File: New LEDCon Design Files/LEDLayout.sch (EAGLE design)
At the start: 23 parts

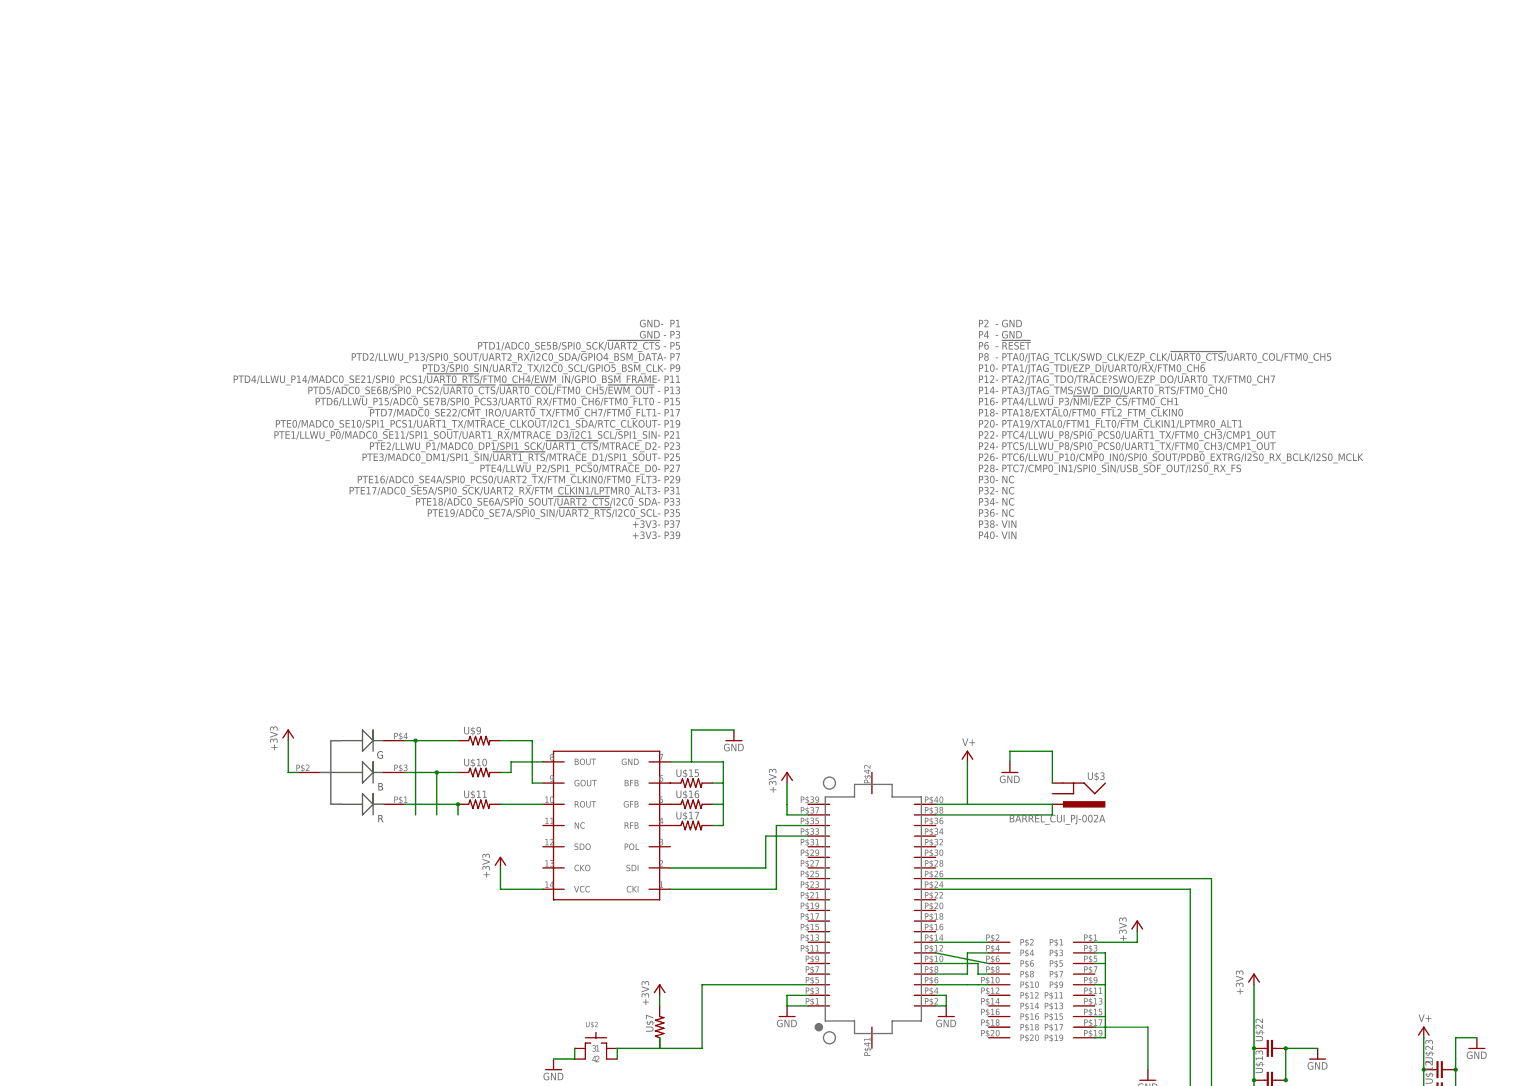
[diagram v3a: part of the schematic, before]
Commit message: Prototype 4
Fixed LED, removed jumpers, fixed JTAG traces and added RA reset button
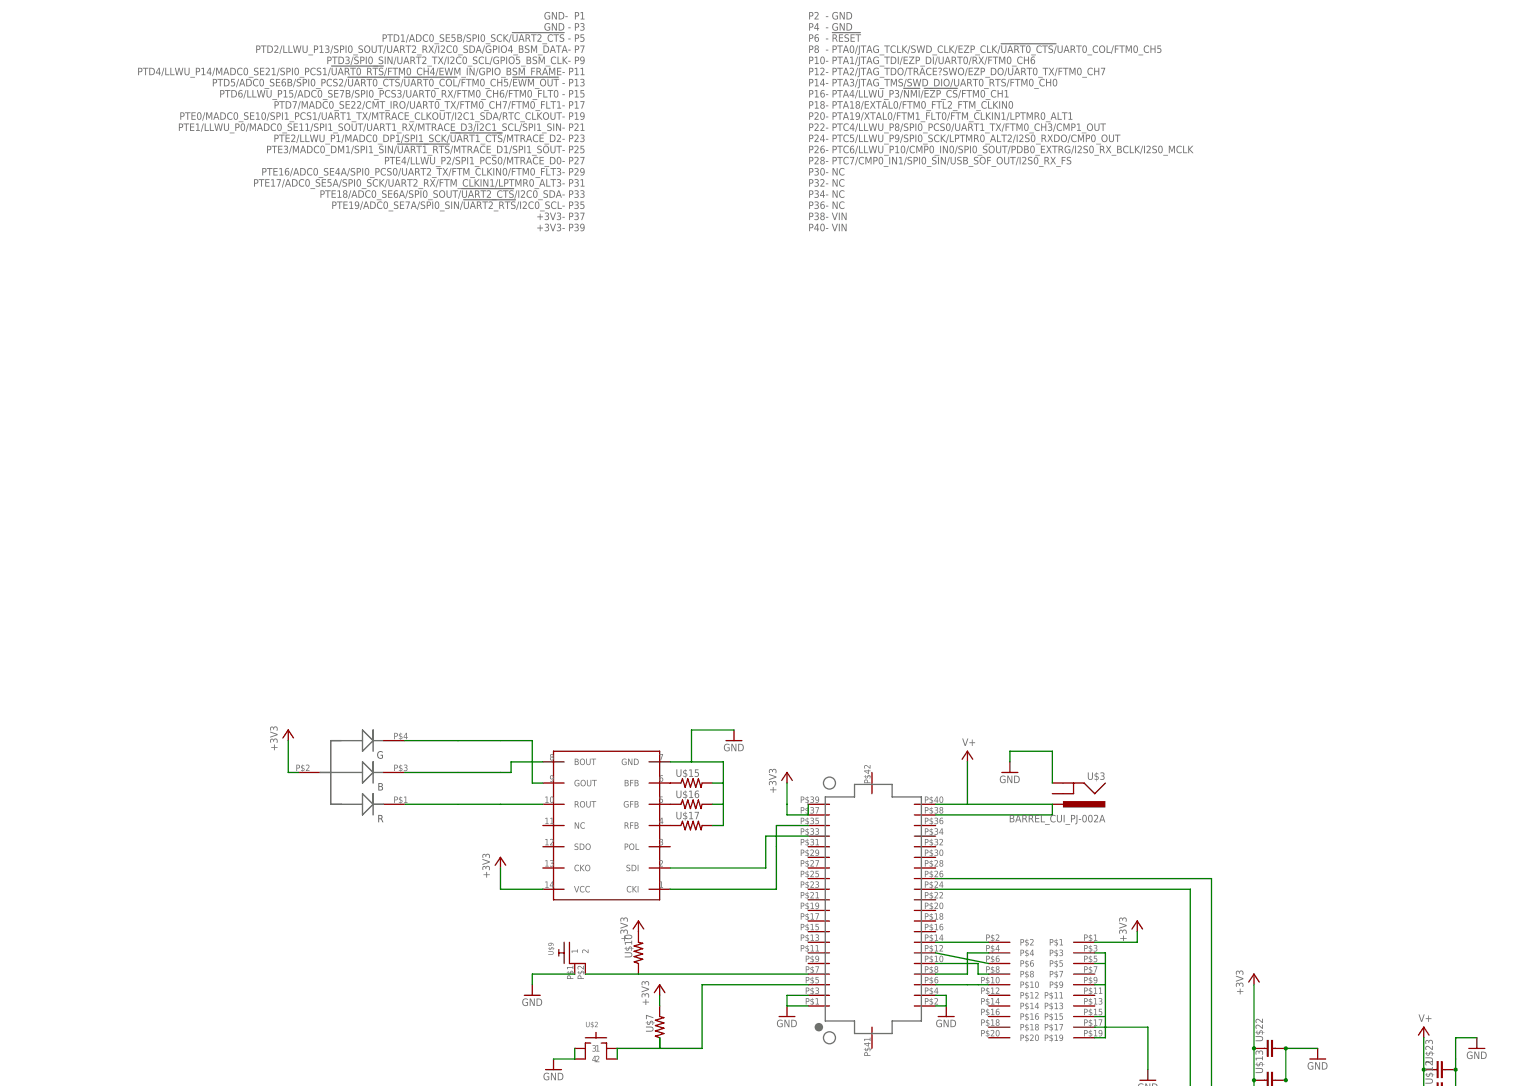
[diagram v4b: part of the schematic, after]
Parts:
- removed U$11: (no value), GW-devices:RF-R0805
- U$9: value (none) -> RA_BUTTON; device GW-devices:RF-R0805 -> KW2:RA_BUTTON
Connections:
- removed net N$19: U$4.PTA3/JTAG_TMS/SWD_DIO/UART0_RTS/FTM0_CH0
- removed net N$22: U$4.PTA2/JTAG_TDO/TRACE?SWO/EZP_DO/UART0_TX/FTM0_CH7
- net +3V3: now also U$10.2, U$4.+3V3@2
- net GND: now also U$9.1
- net N$4: now also U$8.GOUT; no longer U$9.1
- net N$5: now also U$8.BOUT; no longer U$10.1
- net N$6: now also U$19.P$2, U$4.PTA3/JTAG_TMS/SWD_DIO/UART0_RTS/FTM0_CH0; no longer U$11.2, U$8.ROUT
- net N$7: now also U$8.ROUT; no longer U$11.1
- net N$8: now also U$19.P$6, U$4.PTA2/JTAG_TDO/TRACE?SWO/EZP_DO/UART0_TX/FTM0_CH7; no longer U$10.2, U$8.BOUT
- net N$9: now also U$10.1, U$4.PTD2/LLWU_P13/SPI0_SOUT/UART2_RX/I2C0_SDA/GPIO4_BSM_DATA; no longer U$8.GOUT
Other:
- moved on the sheet: U$10
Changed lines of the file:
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@@
 <part name="+3V5" library="supply1" deviceset="+3V3" device=""/>
 <part name="U$8" library="GW-devices" deviceset="WS2801" device=""/>
-<part name="U$9" library="GW-devices" deviceset="RF-R" device="0805"/>
-<part name="U$10" library="GW-devices" deviceset="RF-R" device="0805"/>
-<part name="U$11" library="GW-devices" deviceset="RF-R" device="0805"/>
 <part name="GND7" library="supply1" deviceset="GND" device=""/>
 <part name="+3V6" library="supply1" deviceset="+3V3" device=""/>
@@
 <part name="U$22" library="GW-devices" deviceset="RF-C" device="0805"/>
 <part name="U$23" library="GW-devices" deviceset="RF-C" device="0805"/>
+<part name="U$9" library="KW2" deviceset="RA_BUTTON" device=""/>
+<part name="GND11" library="supply1" deviceset="GND" device=""/>
+<part name="U$10" library="GW-devices" deviceset="RF-R" device="0805"/>
+<part name="+3V8" library="supply1" deviceset="+3V3" device=""/>
 </parts>
 <sheets>
@@
 <instance part="+3V5" gate="G$1" x="-129.54" y="25.4"/>
 <instance part="U$8" gate="G$1" x="-55.88" y="2.54" rot="R180"/>
-<instance part="U$9" gate="G$1" x="-83.82" y="22.86"/>
-<instance part="U$10" gate="G$1" x="-83.82" y="15.24"/>
-<instance part="U$11" gate="G$1" x="-83.82" y="7.62"/>
 <instance part="GND7" gate="1" x="-22.86" y="22.86"/>
 <instance part="+3V6" gate="G$1" x="-78.74" y="-5.08"/>
@@
 <instance part="U$22" gate="G$1" x="104.14" y="-50.8" rot="R90"/>
 <instance part="U$23" gate="G$1" x="144.78" y="-55.88" rot="R90"/>
+<instance part="U$9" gate="G$1" x="-60.96" y="-33.02" rot="MR0"/>
+<instance part="GND11" gate="1" x="-71.12" y="-38.1"/>
+<instance part="U$10" gate="G$1" x="-45.72" y="-27.94" smashed="yes" rot="R90">
+<attribute name="NAME" x="-47.2186" y="-29.21" size="1.778" layer="95" rot="R90"/>
+<attribute name="VALUE" x="-42.418" y="-31.75" size="1.778" layer="96" rot="R90"/>
+</instance>
+<instance part="+3V8" gate="G$1" x="-45.72" y="-20.32"/>
 </instances>
 <busses>
@@
 <junction x="109.22" y="-50.8"/>
 </segment>
+<segment>
+<pinref part="U$9" gate="G$1" pin="1"/>
+<pinref part="GND11" gate="1" pin="GND"/>
+<wire x1="-60.96" y1="-33.02" x2="-71.12" y2="-33.02" width="0.1524" layer="91"/>
+<wire x1="-71.12" y1="-33.02" x2="-71.12" y2="-35.56" width="0.1524" layer="91"/>
+</segment>
 </net>
 <net name="+3V3" class="0">
@@
 <wire x1="-5.08" y1="5.08" x2="-10.16" y2="5.08" width="0.1524" layer="91"/>
 <wire x1="-10.16" y1="5.08" x2="-10.16" y2="7.62" width="0.1524" layer="91"/>
+<pinref part="U$4" gate="G$1" pin="+3V3@2"/>
+<wire x1="-5.08" y1="7.62" x2="-5.08" y2="5.08" width="0.1524" layer="91"/>
 </segment>
 <segment>
@@
 </segment>
 <segment>
-<pinref part="U$5" gate="G$1" pin="ANODE"/>
-<wire x1="-127" y1="15.24" x2="-129.54" y2="15.24" width="0.1524" layer="91"/>
 <pinref part="+3V5" gate="G$1" pin="+3V3"/>
 <wire x1="-129.54" y1="15.24" x2="-129.54" y2="22.86" width="0.1524" layer="91"/>
+<pinref part="U$5" gate="G$1" pin="ANODE"/>
+<wire x1="-129.54" y1="15.24" x2="-127" y2="15.24" width="0.1524" layer="91"/>
 </segment>
 <segment>
@@
 <pinref part="U$19" gate="G$1" pin="P$1"/>
 <wire x1="73.66" y1="-25.4" x2="63.5" y2="-25.4" width="0.1524" layer="91"/>
+</segment>
+<segment>
+<pinref part="U$10" gate="G$1" pin="2"/>
+<pinref part="+3V8" gate="G$1" pin="+3V3"/>
 </segment>
 </net>
@@
 <net name="N$4" class="0">
 <segment>
+<wire x1="-78.74" y1="22.86" x2="-71.12" y2="22.86" width="0.1524" layer="91"/>
+<wire x1="-71.12" y1="22.86" x2="-71.12" y2="12.7" width="0.1524" layer="91"/>
+<pinref part="U$8" gate="G$1" pin="GOUT"/>
+<wire x1="-71.12" y1="12.7" x2="-68.58" y2="12.7" width="0.1524" layer="91"/>
+<wire x1="-88.9" y1="22.86" x2="-78.74" y2="22.86" width="0.1524" layer="91"/>
 <pinref part="U$5" gate="G$1" pin="GREEN"/>
-<wire x1="-101.6" y1="22.86" x2="-99.06" y2="22.86" width="0.1524" layer="91"/>
-<pinref part="U$9" gate="G$1" pin="1"/>
-<wire x1="-99.06" y1="22.86" x2="-88.9" y2="22.86" width="0.1524" layer="91"/>
-<wire x1="-99.06" y1="5.08" x2="-99.06" y2="22.86" width="0.1524" layer="91"/>
-<junction x="-99.06" y="22.86"/>
+<wire x1="-88.9" y1="22.86" x2="-101.6" y2="22.86" width="0.1524" layer="91"/>
 </segment>
 </net>
 <net name="N$5" class="0">
 <segment>
-<pinref part="U$5" gate="G$1" pin="BLUE"/>
-<wire x1="-101.6" y1="15.24" x2="-93.98" y2="15.24" width="0.1524" layer="91"/>
-<pinref part="U$10" gate="G$1" pin="1"/>
-<wire x1="-93.98" y1="15.24" x2="-88.9" y2="15.24" width="0.1524" layer="91"/>
-<wire x1="-93.98" y1="5.08" x2="-93.98" y2="15.24" width="0.1524" layer="91"/>
-<junction x="-93.98" y="15.24"/>
-</segment>
-</net>
-<net name="N$7" class="0">
-<segment>
-<pinref part="U$11" gate="G$1" pin="1"/>
-<wire x1="-88.9" y1="5.08" x2="-88.9" y2="7.62" width="0.1524" layer="91"/>
-<pinref part="U$5" gate="G$1" pin="RED"/>
-<wire x1="-101.6" y1="7.62" x2="-88.9" y2="7.62" width="0.1524" layer="91"/>
-<junction x="-88.9" y="7.62"/>
-</segment>
-</net>
-<net name="N$6" class="0">
-<segment>
-<pinref part="U$11" gate="G$1" pin="2"/>
-<pinref part="U$8" gate="G$1" pin="ROUT"/>
-<wire x1="-78.74" y1="7.62" x2="-68.58" y2="7.62" width="0.1524" layer="91"/>
-</segment>
-</net>
-<net name="N$8" class="0">
-<segment>
-<pinref part="U$10" gate="G$1" pin="2"/>
 <wire x1="-78.74" y1="15.24" x2="-76.2" y2="15.24" width="0.1524" layer="91"/>
 <wire x1="-76.2" y1="15.24" x2="-76.2" y2="17.78" width="0.1524" layer="91"/>
 <pinref part="U$8" gate="G$1" pin="BOUT"/>
 <wire x1="-76.2" y1="17.78" x2="-68.58" y2="17.78" width="0.1524" layer="91"/>
-</segment>
-</net>
-<net name="N$9" class="0">
-<segment>
-<pinref part="U$9" gate="G$1" pin="2"/>
-<wire x1="-78.74" y1="22.86" x2="-71.12" y2="22.86" width="0.1524" layer="91"/>
-<wire x1="-71.12" y1="22.86" x2="-71.12" y2="12.7" width="0.1524" layer="91"/>
-<pinref part="U$8" gate="G$1" pin="GOUT"/>
-<wire x1="-71.12" y1="12.7" x2="-68.58" y2="12.7" width="0.1524" layer="91"/>
+<wire x1="-88.9" y1="15.24" x2="-78.74" y2="15.24" width="0.1524" layer="91"/>
+<pinref part="U$5" gate="G$1" pin="BLUE"/>
+<wire x1="-88.9" y1="15.24" x2="-101.6" y2="15.24" width="0.1524" layer="91"/>
+</segment>
+</net>
+<net name="N$7" class="0">
+<segment>
+<pinref part="U$8" gate="G$1" pin="ROUT"/>
+<wire x1="-78.74" y1="7.62" x2="-68.58" y2="7.62" width="0.1524" layer="91"/>
+<wire x1="-88.9" y1="7.62" x2="-78.74" y2="7.62" width="0.1524" layer="91"/>
+<pinref part="U$5" gate="G$1" pin="RED"/>
+<wire x1="-88.9" y1="7.62" x2="-101.6" y2="7.62" width="0.1524" layer="91"/>
 </segment>
 </net>
@@
 </segment>
 </net>
-<net name="N$19" class="0">
-<segment>
-<pinref part="U$4" gate="G$1" pin="PTA3/JTAG_TMS/SWD_DIO/UART0_RTS/FTM0_CH0"/>
-<wire x1="25.4" y1="-25.4" x2="38.1" y2="-25.4" width="0.1524" layer="91"/>
-</segment>
-</net>
 <net name="N$18" class="0">
 <segment>
@@
 </segment>
 </net>
-<net name="N$22" class="0">
+<net name="N$6" class="0">
+<segment>
+<pinref part="U$4" gate="G$1" pin="PTA3/JTAG_TMS/SWD_DIO/UART0_RTS/FTM0_CH0"/>
+<pinref part="U$19" gate="G$1" pin="P$2"/>
+<wire x1="25.4" y1="-25.4" x2="38.1" y2="-25.4" width="0.1524" layer="91"/>
+</segment>
+</net>
+<net name="N$8" class="0">
 <segment>
 <pinref part="U$4" gate="G$1" pin="PTA2/JTAG_TDO/TRACE?SWO/EZP_DO/UART0_TX/FTM0_CH7"/>
+<pinref part="U$19" gate="G$1" pin="P$6"/>
 <wire x1="25.4" y1="-27.94" x2="38.1" y2="-30.48" width="0.1524" layer="91"/>
 </segment>
 </net>
+<net name="N$9" class="0">
+<segment>
+<pinref part="U$9" gate="G$1" pin="2"/>
+<pinref part="U$4" gate="G$1" pin="PTD2/LLWU_P13/SPI0_SOUT/UART2_RX/I2C0_SDA/GPIO4_BSM_DATA"/>
+<wire x1="-58.42" y1="-33.02" x2="-45.72" y2="-33.02" width="0.1524" layer="91"/>
+<pinref part="U$10" gate="G$1" pin="1"/>
+<wire x1="-45.72" y1="-33.02" x2="-5.08" y2="-33.02" width="0.1524" layer="91"/>
+</segment>
+</net>

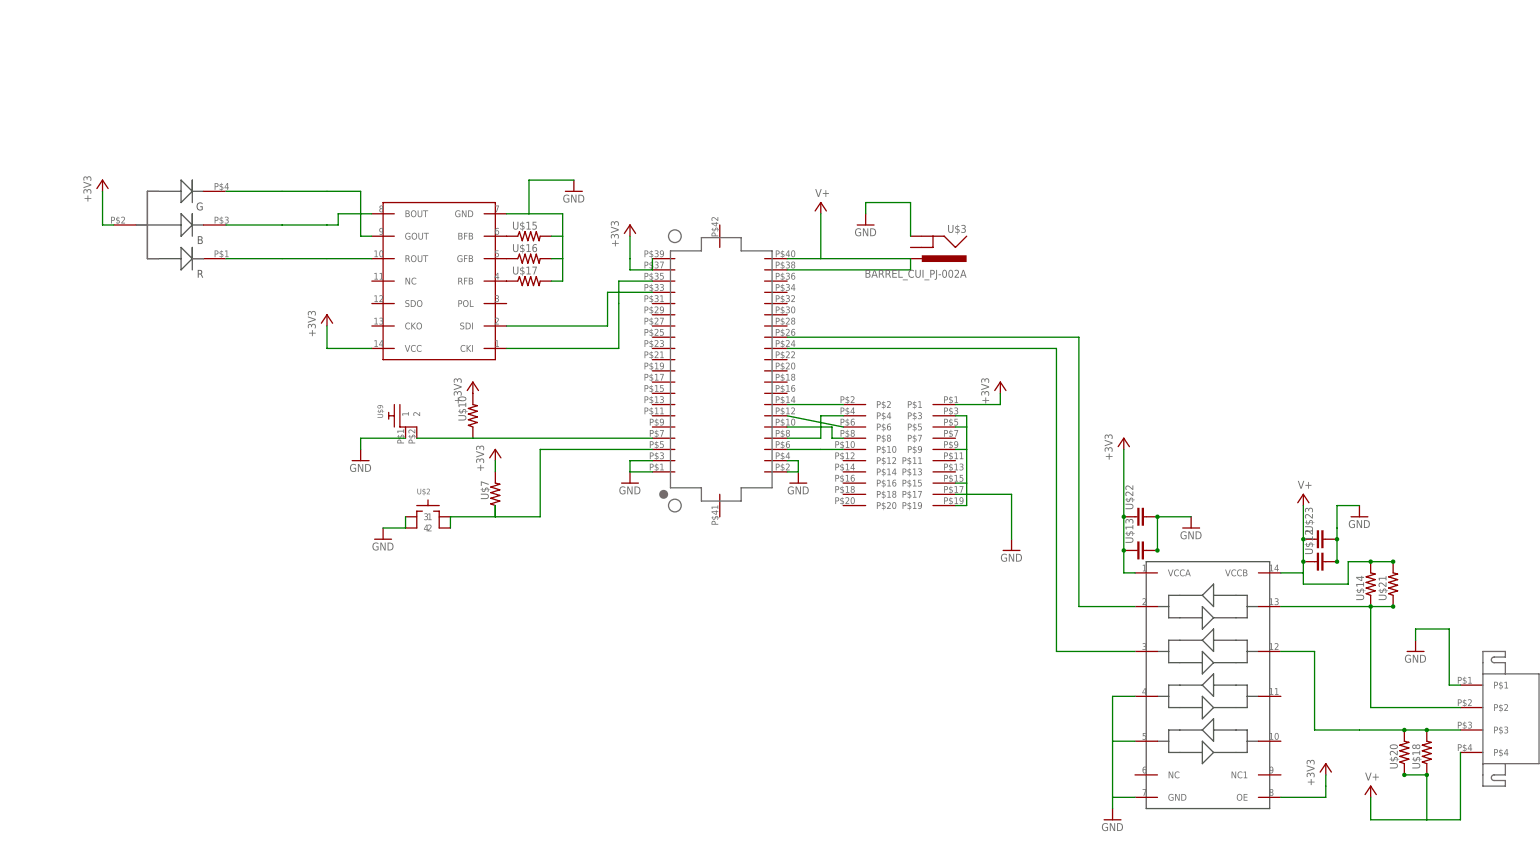
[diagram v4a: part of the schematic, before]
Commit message: Prototype 5
Added Vreg, caps, fixed LED, assigned values & PNs, removed 0402
footprints. Pending exporting of production files
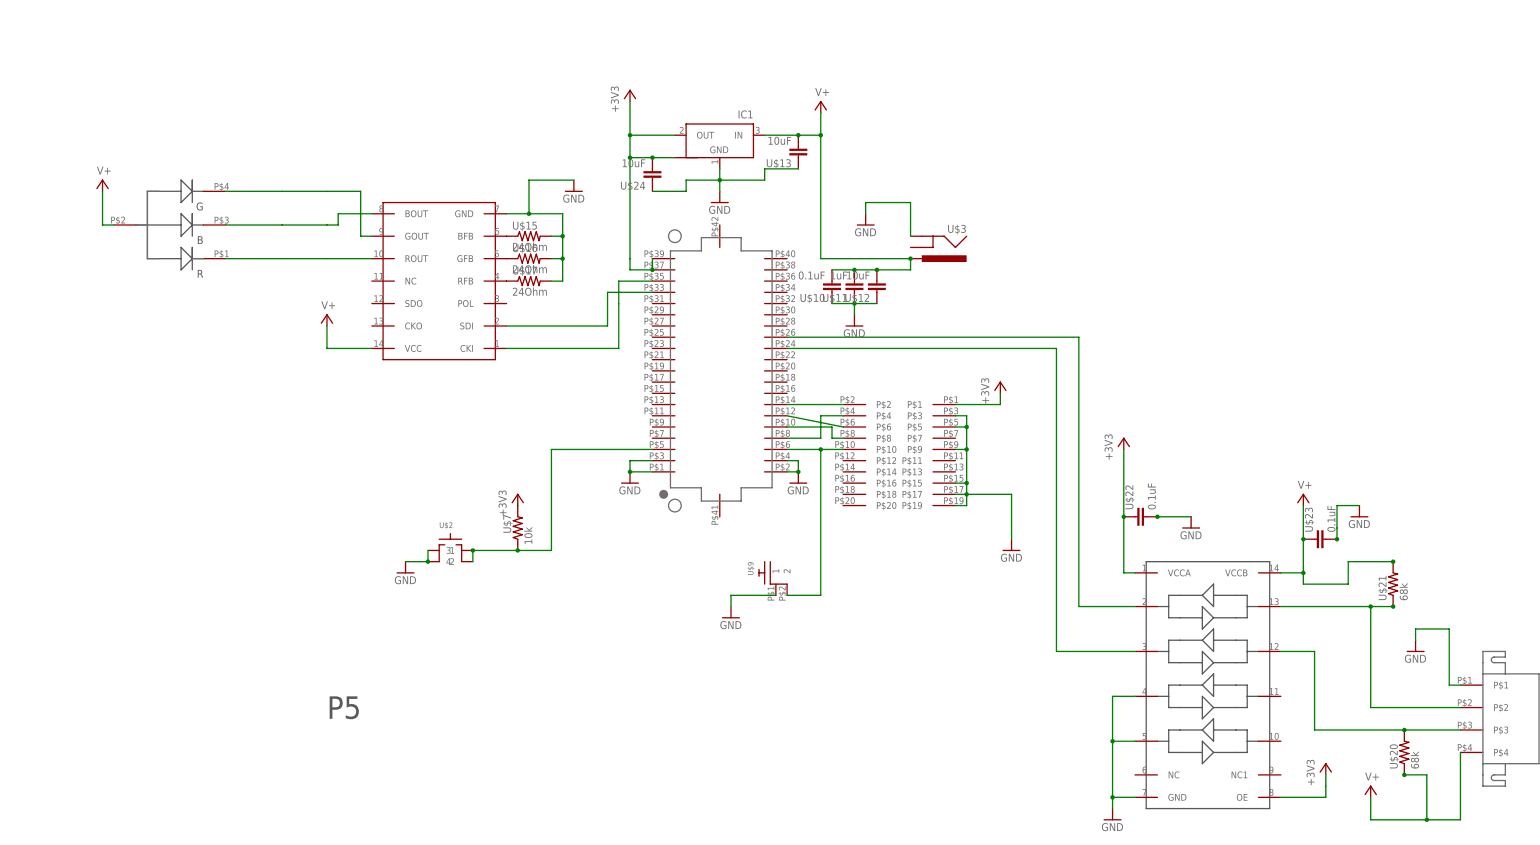
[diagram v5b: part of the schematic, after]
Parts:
- removed U$14, U$18: (no value), GW-devices:RF-R0402
- added IC1: (no value), KW2:NCP1117ST33T3G_1
- added U$11: 1uF, GW-devices:RF-C0805
- added U$24: 10uF, GW-devices:RF-C0805
- U$1: MFGN (none) -> TE Connectivity; MFGP (none) -> 643230-1
- U$10: value (none) -> 0.1uF; device GW-devices:RF-R0805 -> GW-devices:RF-C0805; MFGN (none) -> TDK; MFGP (none) -> C2012X5R1H104K085AA
- U$12, U$13: value (none) -> 10uF; device GW-devices:RF-C0402 -> GW-devices:RF-C0805; MFGN (none) -> Murata; MFGP (none) -> GRM219R61E106KA12D
- U$15, U$16, U$17: value (none) -> 24Ohm; MFGN (none) -> Vishay Dale; MFGP (none) -> CRCW080524R0FKEA
- U$2: MFGN (none) -> E-Switch; MFGP (none) -> TL3301PF160QG
- U$20, U$21: value (none) -> 68k; MFGN (none) -> Vishay Dale; MFGP (none) -> CRCW080568K0FKEA
- U$22, U$23: value (none) -> 0.1uF; MFGN (none) -> TDK; MFGP (none) -> C2012X5R1H104K085AA
- U$4: MFGN (none) -> Hirose; MFGP (none) -> DF12(3.0)-40DP-0.5V(86)
- U$5: MFGN Cree, Inc -> (none); MFGP CLV1A-FKB-CK1N1G1BB7R4S3 -> (none)
- U$6: MFGN (none) -> Texas Instruments
- U$7: value (none) -> 10k; MFGN (none) -> Vishay Dale; MFGP (none) -> CRCW080510K0FKEA
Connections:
- removed net N$21 (its old number): U$19.P$10, U$4.!RESET
- removed net N$9: U$10.1, U$4.PTD2/LLWU_P13/SPI0_SOUT/UART2_RX/I2C0_SDA/GPIO4_BSM_DATA, U$9.2
- new net N$3: U$19.P$10, U$4.!RESET, U$9.2
- net +3V3: now also IC1.OUT, IC1.OUT1, U$24.2; no longer U$10.2, U$13.1, U$5.ANODE, U$8.VCC
- net CLK_5V: no longer U$18.2
- net DAT_5V: no longer U$14.1
- net GND: now also IC1.GND, U$10.1, U$11.1, U$12.1, U$13.1, U$24.1; no longer U$12.2, U$13.2
- net V+: now also IC1.IN, U$10.2, U$11.2, U$12.2, U$13.2, U$5.ANODE, U$8.VCC; no longer U$12.1, U$14.2, U$18.1, U$4.VIN@1, U$4.VIN@2
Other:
- note added: "P5"
- moved on the sheet: U$12, U$13, U$2, U$7, U$9
